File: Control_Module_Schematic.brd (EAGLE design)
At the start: 67 x 47 mm, 30 parts, among them U2 ATMEGA328P_TQFP

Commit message: Connected the FTDI232 UART chip's GND to GND
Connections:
- net GND: now also FTDI232.6
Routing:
- net GND: track 212.5 -> 237.6 mm
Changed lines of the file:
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@@
 <wire x1="54.4576" y1="27.0256" x2="54.3392" y2="27.0683" width="0.254" layer="1"/>
 <via x="35.9664" y="28.8544" extent="1-16" drill="0.3302"/>
+<contactref element="FTDI232" pad="6"/>
+<wire x1="27.8892" y1="32.9184" x2="27.8892" y2="31.7754" width="0.254" layer="1"/>
+<wire x1="21.2598" y1="39.5478" x2="27.8892" y2="32.9184" width="0.254" layer="1"/>
+<wire x1="21.2598" y1="41.8338" x2="21.2598" y2="39.5478" width="0.254" layer="1"/>
+<wire x1="20.1168" y1="42.9768" x2="21.2598" y2="41.8338" width="0.254" layer="1"/>
+<wire x1="14.6304" y1="42.9768" x2="20.1168" y2="42.9768" width="0.254" layer="1"/>
+<wire x1="11.2014" y1="39.5478" x2="14.6304" y2="42.9768" width="0.254" layer="1"/>
+<wire x1="27.8892" y1="31.7754" x2="27.94" y2="31.7246" width="0.254" layer="1"/>
+<wire x1="11.2014" y1="39.5478" x2="11.06" y2="39.37" width="0.254" layer="1"/>
 </signal>
 <signal name="N$5">

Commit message: AC solid state relay pin change
The AC SSR is now controlled by pc2 from the atmega328. The previous pin
used to control it ADC7 was not capable of producing output and it has
been rerouted to the breakout header.
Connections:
- removed net PC2: JP4.2, U2.25
- new net ADC7: JP4.2, U2.22
- net N$9: now also U2.25; no longer U2.22
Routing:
- net ADC7: track 0.00 -> 63.2 mm, vias 0 -> 3
- net N$9: track 9.58 -> 45.4 mm
- net PC2: track 28.3 -> 0.00 mm, vias 1 -> 0
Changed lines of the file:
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@@
 </class>
 </classes>
-<designrules name="oshpark-2layer">
-<description language="de">&lt;b&gt;EAGLE Design Rules&lt;/b&gt;
+<designrules name="SparkFun">
+<description language="en">&lt;b&gt;EAGLE Design Rules&lt;/b&gt;
 &lt;p&gt;
-Die Standard-Design-Rules sind so gewählt, dass sie für
-die meisten Anwendungen passen. Sollte ihre Platine
-besondere Anforderungen haben, treffen Sie die erforderlichen
-Einstellungen hier und speichern die Design Rules unter
-einem neuen Namen ab.</description>
-<description language="en">&lt;b&gt;Laen's PCB Order Design Rules&lt;/b&gt;
-&lt;p&gt;
-Please make sure your boards conform to these design rules.</description>
+The default Design Rules have been set to cover
+a wide range of applications. Your particular design
+may have different requirements, so please make the
+necessary adjustments and save your customized
+design rules under a new name.</description>
 <param name="layerSetup" value="(1*16)"/>
-<param name="mtCopper" value="0.0356mm 0.0356mm 0.0356mm 0.0356mm 0.0356mm 0.0356mm 0.0356mm 0.0356mm 0.0356mm 0.0356mm 0.0356mm 0.0356mm 0.0356mm 0.0356mm 0.0356mm 0.0356mm"/>
-<param name="mtIsolate" value="1.5011mm 0.1499mm 0.2007mm 0.1499mm 0.2007mm 0.1499mm 0.2007mm 0.1499mm 0.2007mm 0.1499mm 0.2007mm 0.1499mm 0.2007mm 0.1499mm 0.2007mm"/>
-<param name="mdWireWire" value="6mil"/>
-<param name="mdWirePad" value="6mil"/>
-<param name="mdWireVia" value="6mil"/>
-<param name="mdPadPad" value="6mil"/>
-<param name="mdPadVia" value="6mil"/>
-<param name="mdViaVia" value="6mil"/>
-<param name="mdSmdPad" value="6mil"/>
-<param name="mdSmdVia" value="6mil"/>
-<param name="mdSmdSmd" value="6mil"/>
+<param name="mtCopper" value="0.035mm 0.035mm 0.035mm 0.035mm 0.035mm 0.035mm 0.035mm 0.035mm 0.035mm 0.035mm 0.035mm 0.035mm 0.035mm 0.035mm 0.035mm 0.035mm"/>
+<param name="mtIsolate" value="1.5mm 0.15mm 0.2mm 0.15mm 0.2mm 0.15mm 0.2mm 0.15mm 0.2mm 0.15mm 0.2mm 0.15mm 0.2mm 0.15mm 0.2mm"/>
+<param name="mdWireWire" value="8mil"/>
+<param name="mdWirePad" value="8mil"/>
+<param name="mdWireVia" value="8mil"/>
+<param name="mdPadPad" value="8mil"/>
+<param name="mdPadVia" value="8mil"/>
+<param name="mdViaVia" value="8mil"/>
+<param name="mdSmdPad" value="8mil"/>
+<param name="mdSmdVia" value="8mil"/>
+<param name="mdSmdSmd" value="8mil"/>
 <param name="mdViaViaSameLayer" value="8mil"/>
 <param name="mnLayersViaInSmd" value="2"/>
-<param name="mdCopperDimension" value="15mil"/>
-<param name="mdDrill" value="6mil"/>
+<param name="mdCopperDimension" value="8mil"/>
+<param name="mdDrill" value="8mil"/>
 <param name="mdSmdStop" value="0mil"/>
-<param name="msWidth" value="6mil"/>
-<param name="msDrill" value="13mil"/>
-<param name="msMicroVia" value="13mil"/>
+<param name="msWidth" value="8mil"/>
+<param name="msDrill" value="20mil"/>
+<param name="msMicroVia" value="9.99mm"/>
 <param name="msBlindViaRatio" value="0.5"/>
 <param name="rvPadTop" value="0.25"/>
@@
 <param name="rvMicroViaOuter" value="0.25"/>
 <param name="rvMicroViaInner" value="0.25"/>
-<param name="rlMinPadTop" value="7mil"/>
+<param name="rlMinPadTop" value="12mil"/>
 <param name="rlMaxPadTop" value="20mil"/>
-<param name="rlMinPadInner" value="7mil"/>
+<param name="rlMinPadInner" value="10mil"/>
 <param name="rlMaxPadInner" value="20mil"/>
-<param name="rlMinPadBottom" value="7mil"/>
+<param name="rlMinPadBottom" value="12mil"/>
 <param name="rlMaxPadBottom" value="20mil"/>
-<param name="rlMinViaOuter" value="7mil"/>
+<param name="rlMinViaOuter" value="10mil"/>
 <param name="rlMaxViaOuter" value="20mil"/>
-<param name="rlMinViaInner" value="7mil"/>
+<param name="rlMinViaInner" value="10mil"/>
 <param name="rlMaxViaInner" value="20mil"/>
 <param name="rlMinMicroViaOuter" value="4mil"/>
@@
 <param name="mlMinCreamFrame" value="0mil"/>
 <param name="mlMaxCreamFrame" value="0mil"/>
-<param name="mlViaStopLimit" value="0mil"/>
+<param name="mlViaStopLimit" value="20mil"/>
 <param name="srRoundness" value="0"/>
 <param name="srMinRoundness" value="0mil"/>
@@
 <wire x1="54.2544" y1="29.464" x2="54.3392" y2="29.6083" width="0.254" layer="1"/>
 </signal>
-<signal name="N$9">
-<contactref element="R1" pad="1"/>
-<contactref element="U2" pad="22"/>
-<wire x1="39.624" y1="21.5392" x2="38.608" y2="21.5392" width="0.254" layer="1"/>
-<wire x1="44.704" y1="26.6192" x2="39.624" y2="21.5392" width="0.254" layer="1"/>
-<wire x1="45.9232" y1="26.6192" x2="44.704" y2="26.6192" width="0.254" layer="1"/>
-<wire x1="38.608" y1="21.5392" x2="38.5826" y2="21.52" width="0.254" layer="1"/>
-<wire x1="45.9232" y1="26.6192" x2="46.04" y2="26.67" width="0.254" layer="1"/>
-</signal>
 <signal name="N$11">
 <contactref element="SSR" pad="P$2"/>
@@
 <wire x1="54.5846" y1="42.6466" x2="54.3392" y2="42.1583" width="2.921" layer="1"/>
 <wire x1="62.1792" y1="42.8752" x2="62.23" y2="43.02" width="2.921" layer="1"/>
-</signal>
-<signal name="PC2">
-<contactref element="JP4" pad="2"/>
-<contactref element="U2" pad="25"/>
-<wire x1="37.5666" y1="25.8572" x2="37.1856" y2="24.7904" width="0.254" layer="1"/>
-<wire x1="37.3888" y1="27.3304" x2="37.5666" y2="25.8572" width="0.254" layer="1"/>
-<wire x1="37.5666" y1="25.8064" x2="37.3888" y2="27.3304" width="0.254" layer="16"/>
-<wire x1="36.9824" y1="25.6032" x2="37.5666" y2="25.8064" width="0.254" layer="16"/>
-<wire x1="36.576" y1="25.6032" x2="36.9824" y2="25.6032" width="0.254" layer="16"/>
-<wire x1="29.2608" y1="32.9184" x2="36.576" y2="25.6032" width="0.254" layer="16"/>
-<wire x1="29.2608" y1="33.1216" x2="29.2608" y2="32.9184" width="0.254" layer="16"/>
-<wire x1="23.368" y1="39.0144" x2="29.2608" y2="33.1216" width="0.254" layer="16"/>
-<wire x1="21.5392" y1="39.0144" x2="23.368" y2="39.0144" width="0.254" layer="16"/>
-<wire x1="20.1168" y1="40.4368" x2="21.5392" y2="39.0144" width="0.254" layer="16"/>
-<wire x1="37.1856" y1="24.7904" x2="37.09" y2="24.6126" width="0.254" layer="1"/>
-<wire x1="20.1168" y1="40.4368" x2="19.9517" y2="40.6146" width="0.254" layer="16"/>
-<via x="37.3888" y="27.3304" extent="1-16" drill="0.3302"/>
 </signal>
 <signal name="PC3">
@@
 <wire x1="34.925" y1="19.0754" x2="34.9504" y2="19.1008" width="0.254" layer="16"/>
 </signal>
+<signal name="N$9">
+<contactref element="U2" pad="25"/>
+<contactref element="R1" pad="1"/>
+<wire x1="37.2618" y1="25.8318" x2="37.2618" y2="24.6888" width="0.254" layer="1"/>
+<wire x1="37.4904" y1="26.0604" x2="37.2618" y2="25.8318" width="0.254" layer="1"/>
+<wire x1="37.4904" y1="35.6616" x2="37.4904" y2="26.0604" width="0.254" layer="1"/>
+<wire x1="33.8328" y1="39.3192" x2="37.4904" y2="35.6616" width="0.254" layer="1"/>
+<wire x1="33.8328" y1="41.8338" x2="33.8328" y2="39.3192" width="0.254" layer="1"/>
+<wire x1="35.8902" y1="43.8912" x2="33.8328" y2="41.8338" width="0.254" layer="1"/>
+<wire x1="39.5478" y1="43.8912" x2="35.8902" y2="43.8912" width="0.254" layer="1"/>
+<wire x1="45.9486" y1="37.4904" x2="39.5478" y2="43.8912" width="0.254" layer="1"/>
+<wire x1="45.9486" y1="26.7462" x2="45.9486" y2="37.4904" width="0.254" layer="1"/>
+<wire x1="37.2618" y1="24.6888" x2="37.09" y2="24.6126" width="0.254" layer="1"/>
+<wire x1="45.9486" y1="26.7462" x2="46.04" y2="26.67" width="0.254" layer="1"/>
+</signal>
+<signal name="ADC7">
+<contactref element="U2" pad="22"/>
+<contactref element="JP4" pad="2"/>
+<wire x1="39.3192" y1="21.4884" x2="38.6334" y2="21.4884" width="0.254" layer="1"/>
+<wire x1="44.1198" y1="26.289" x2="39.3192" y2="21.4884" width="0.254" layer="1"/>
+<wire x1="44.1198" y1="34.29" x2="44.1198" y2="26.289" width="0.254" layer="1"/>
+<wire x1="39.0906" y1="39.3192" x2="44.1198" y2="34.29" width="0.254" layer="1"/>
+<wire x1="39.0906" y1="42.9768" x2="39.0906" y2="39.3192" width="0.254" layer="1"/>
+<wire x1="38.6334" y1="42.9768" x2="39.0906" y2="42.9768" width="0.254" layer="16"/>
+<wire x1="37.9476" y1="43.6626" x2="38.6334" y2="42.9768" width="0.254" layer="16"/>
+<wire x1="16.6878" y1="43.6626" x2="37.9476" y2="43.6626" width="0.254" layer="16"/>
+<wire x1="13.2588" y1="40.2336" x2="16.6878" y2="43.6626" width="0.254" layer="16"/>
+<wire x1="15.5448" y1="40.2336" x2="13.2588" y2="40.2336" width="0.254" layer="1"/>
+<wire x1="17.8308" y1="37.9476" x2="15.5448" y2="40.2336" width="0.254" layer="1"/>
+<wire x1="18.0594" y1="37.9476" x2="17.8308" y2="37.9476" width="0.254" layer="1"/>
+<wire x1="18.0594" y1="38.4048" x2="18.0594" y2="37.9476" width="0.254" layer="16"/>
+<wire x1="20.1168" y1="40.4622" x2="18.0594" y2="38.4048" width="0.254" layer="16"/>
+<wire x1="38.6334" y1="21.4884" x2="38.5826" y2="21.52" width="0.254" layer="1"/>
+<wire x1="20.1168" y1="40.4622" x2="19.9517" y2="40.6146" width="0.254" layer="16"/>
+<via x="39.0906" y="42.9768" extent="1-16" drill="0.508"/>
+<via x="13.2588" y="40.2336" extent="1-16" drill="0.508"/>
+<via x="18.0594" y="37.9476" extent="1-16" drill="0.508"/>
+</signal>
 </signals>

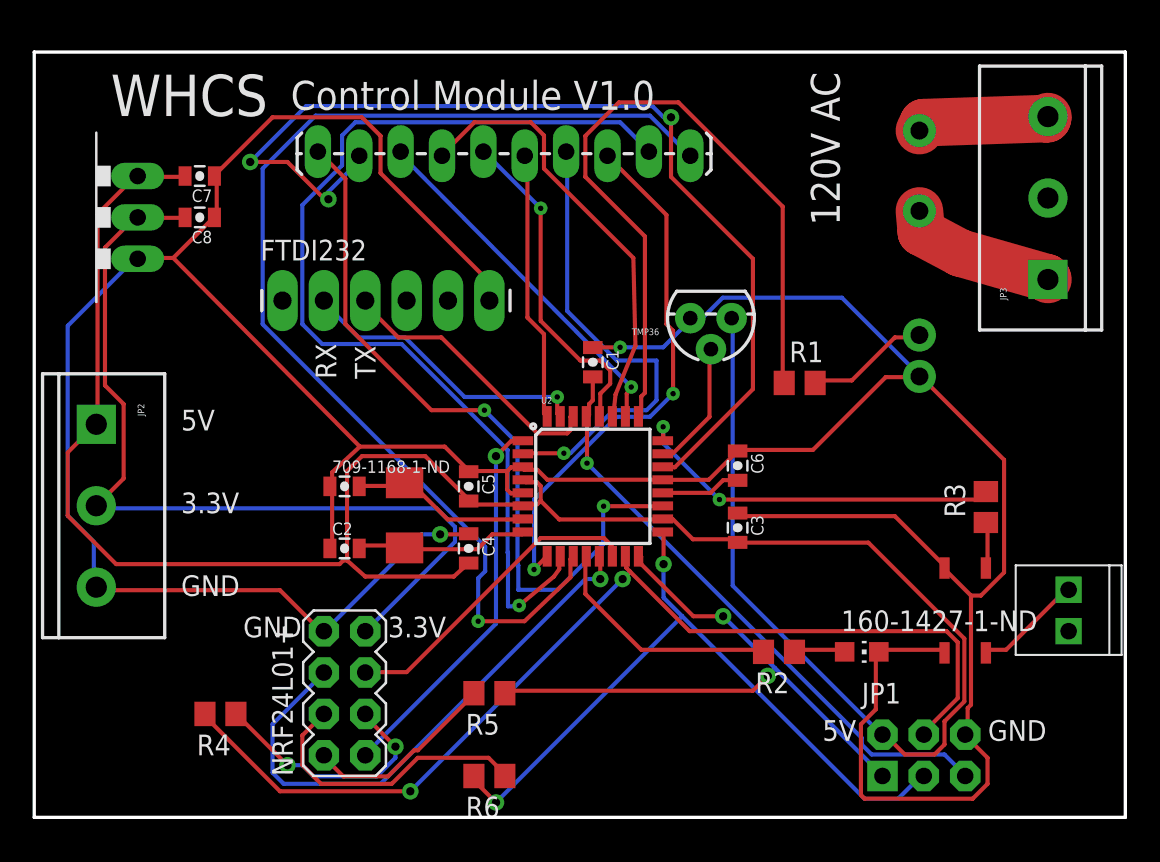
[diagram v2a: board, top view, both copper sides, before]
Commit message: Added tactile switch for reset
Also did some manual routing optimizations
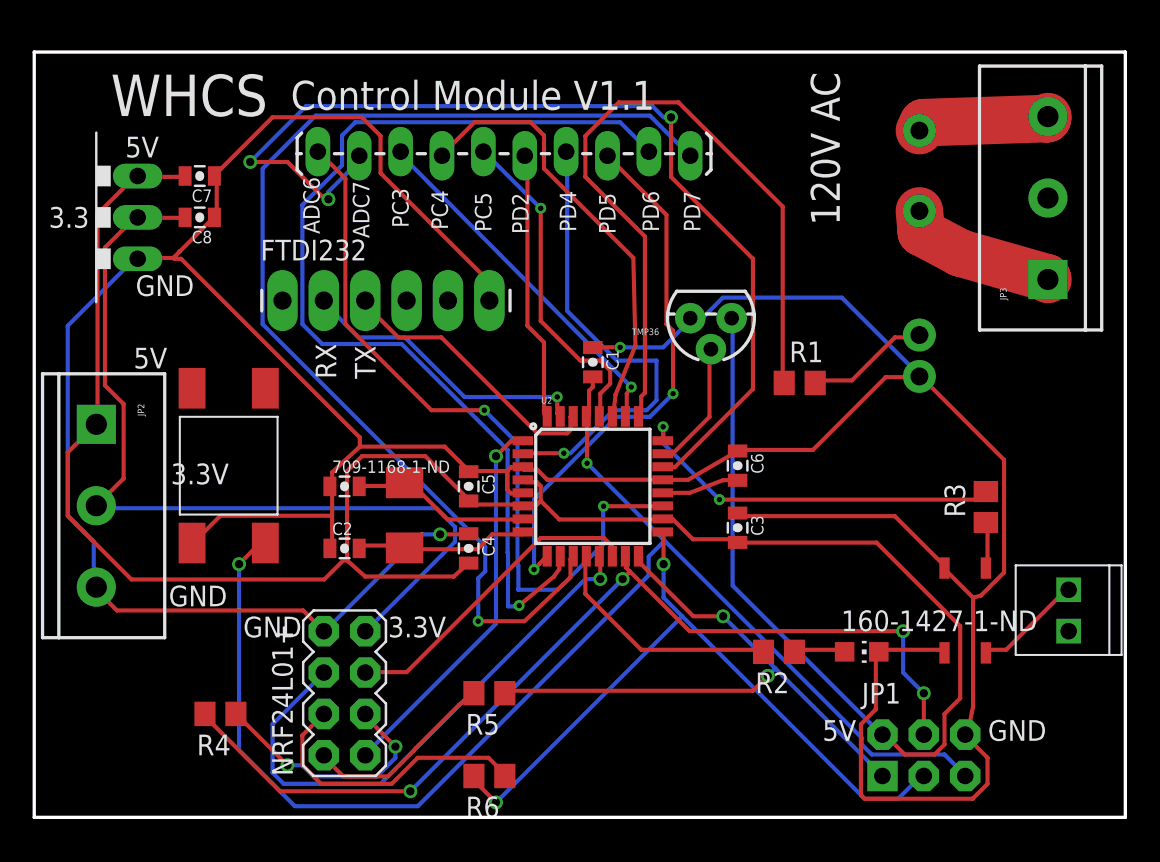
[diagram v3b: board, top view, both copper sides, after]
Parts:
- added TAC_SWITCH: TACTILE_SWITCH, WHCS:TAC_SWITCH_GULL_WING
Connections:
- net GND: now also TAC_SWITCH.P$2
- net N$24: now also TAC_SWITCH.P$4
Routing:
- net N$24: track 37.0 -> 85.6 mm, vias 1 -> 2
- net GND: track 237.6 -> 247.1 mm
- net N$3: track 63.2 -> 60.1 mm, vias 2 -> 4
- net 5V: track 144.3 -> 145.2 mm
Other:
- board text added: "3.3"
- board text added: "ADC6"
- board text added: "ADC7"
- board text added: "Control Module V1.1"
- board text added: "PC3"
- board text added: "PC4"
- board text added: "PC5"
- board text added: "PD2"
- board text added: "PD4"
- board text added: "PD5"
- board text added: "PD6"
- board text added: "PD7"
- board text removed: "Control Module V1.0"

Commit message: Final changes before placing oshpark 2nd order.
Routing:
- net ADC7: track 63.2 -> 69.5 mm
- net N$9: track 45.4 -> 47.7 mm
- net PD7: track 70.4 -> 71.4 mm
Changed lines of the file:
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@@
 <text x="6.223" y="32.004" size="1.27" layer="21">GND</text>
 <text x="0.889" y="36.195" size="1.27" layer="21">3.3</text>
+<text x="27.305" y="29.337" size="1.27" layer="21" rot="R270">GND</text>
 </plain>
 <attributes>
@@
 <contactref element="JP4" pad="5"/>
 <contactref element="U2" pad="28"/>
-<wire x1="34.7472" y1="26.0096" x2="34.7472" y2="24.7904" width="0.254" layer="1"/>
-<wire x1="35.3568" y1="26.6192" x2="34.7472" y2="26.0096" width="0.254" layer="1"/>
+<wire x1="34.7472" y1="25.8826" x2="34.7472" y2="24.7904" width="0.254" layer="1"/>
+<wire x1="35.3568" y1="26.6192" x2="34.7472" y2="25.8826" width="0.254" layer="1"/>
 <wire x1="35.3568" y1="27.432" x2="35.3568" y2="26.6192" width="0.254" layer="1"/>
 <wire x1="34.7472" y1="28.0416" x2="35.3568" y2="27.432" width="0.254" layer="1"/>
@@
 <wire x1="31.9024" y1="14.7828" x2="29.7688" y2="13.0048" width="0.254" layer="1"/>
 <wire x1="29.0576" y1="22.5552" x2="29.0576" y2="16.256" width="0.254" layer="16"/>
-<wire x1="22.5552" y1="29.0576" x2="29.0576" y2="22.5552" width="0.254" layer="16"/>
-<wire x1="17.6784" y1="29.0576" x2="22.5552" y2="29.0576" width="0.254" layer="16"/>
-<wire x1="16.4592" y1="30.2768" x2="17.6784" y2="29.0576" width="0.254" layer="16"/>
+<wire x1="22.5552" y1="28.8036" x2="29.0576" y2="22.5552" width="0.254" layer="16"/>
+<wire x1="17.8054" y1="28.8036" x2="22.5552" y2="28.8036" width="0.254" layer="16"/>
+<wire x1="16.4592" y1="30.2768" x2="17.8054" y2="28.8036" width="0.254" layer="16"/>
 <wire x1="16.4592" y1="37.592" x2="16.4592" y2="30.2768" width="0.254" layer="16"/>
 <wire x1="18.8976" y1="40.0304" x2="16.4592" y2="37.592" width="0.254" layer="16"/>
@@
 <wire x1="14.0208" y1="30.2768" x2="27.686" y2="16.6116" width="0.254" layer="16"/>
 <wire x1="14.0208" y1="39.8272" x2="14.0208" y2="30.2768" width="0.254" layer="16"/>
-<wire x1="17.272" y1="43.0784" x2="14.0208" y2="39.8272" width="0.254" layer="16"/>
-<wire x1="37.7952" y1="43.0784" x2="17.272" y2="43.0784" width="0.254" layer="16"/>
-<wire x1="40.2336" y1="40.64" x2="37.7952" y2="43.0784" width="0.254" layer="16"/>
+<wire x1="18.288" y1="44.0944" x2="14.0208" y2="39.8272" width="0.254" layer="16"/>
+<wire x1="37.2872" y1="44.0944" x2="18.288" y2="44.0944" width="0.254" layer="16"/>
+<wire x1="40.2336" y1="40.64" x2="37.2872" y2="44.0944" width="0.254" layer="16"/>
 <wire x1="32.9184" y1="15.8496" x2="33.09" y2="16.0274" width="0.254" layer="1"/>
 <wire x1="40.2336" y1="40.64" x2="40.2717" y2="40.6146" width="0.254" layer="16"/>
@@
 <wire x1="33.8328" y1="39.3192" x2="37.4904" y2="35.6616" width="0.254" layer="1"/>
 <wire x1="33.8328" y1="41.8338" x2="33.8328" y2="39.3192" width="0.254" layer="1"/>
-<wire x1="35.8902" y1="43.8912" x2="33.8328" y2="41.8338" width="0.254" layer="1"/>
-<wire x1="39.5478" y1="43.8912" x2="35.8902" y2="43.8912" width="0.254" layer="1"/>
-<wire x1="45.9486" y1="37.4904" x2="39.5478" y2="43.8912" width="0.254" layer="1"/>
+<wire x1="36.3982" y1="44.5262" x2="33.8328" y2="41.8338" width="0.254" layer="1"/>
 <wire x1="45.9486" y1="26.7462" x2="45.9486" y2="37.4904" width="0.254" layer="1"/>
 <wire x1="37.2618" y1="24.6888" x2="37.09" y2="24.6126" width="0.254" layer="1"/>
 <wire x1="45.9486" y1="26.7462" x2="46.04" y2="26.67" width="0.254" layer="1"/>
+<wire x1="36.3982" y1="44.5262" x2="41.8338" y2="44.5262" width="0.254" layer="1"/>
+<wire x1="41.8338" y1="44.5262" x2="45.72" y2="40.64" width="0.254" layer="1"/>
+<wire x1="45.72" y1="40.64" x2="45.72" y2="37.719" width="0.254" layer="1"/>
+<wire x1="45.72" y1="37.719" x2="45.9486" y2="37.4904" width="0.254" layer="1"/>
 </signal>
 <signal name="ADC7">
@@
 <wire x1="44.1198" y1="34.29" x2="44.1198" y2="26.289" width="0.254" layer="1"/>
 <wire x1="39.0906" y1="39.3192" x2="44.1198" y2="34.29" width="0.254" layer="1"/>
-<wire x1="39.0906" y1="42.9768" x2="39.0906" y2="39.3192" width="0.254" layer="1"/>
-<wire x1="38.6334" y1="42.9768" x2="39.0906" y2="42.9768" width="0.254" layer="16"/>
-<wire x1="37.9476" y1="43.6626" x2="38.6334" y2="42.9768" width="0.254" layer="16"/>
-<wire x1="16.6878" y1="43.6626" x2="37.9476" y2="43.6626" width="0.254" layer="16"/>
-<wire x1="13.2588" y1="40.2336" x2="16.6878" y2="43.6626" width="0.254" layer="16"/>
+<wire x1="39.0906" y1="43.6118" x2="39.0906" y2="39.3192" width="0.254" layer="1"/>
+<wire x1="39.0144" y1="44.8818" x2="39.0906" y2="43.6118" width="0.254" layer="16"/>
+<wire x1="17.9578" y1="44.9326" x2="37.9476" y2="44.9326" width="0.254" layer="16"/>
+<wire x1="13.2588" y1="40.2336" x2="17.9578" y2="44.9326" width="0.254" layer="16"/>
 <wire x1="15.5448" y1="40.2336" x2="13.2588" y2="40.2336" width="0.254" layer="1"/>
 <wire x1="17.8308" y1="37.9476" x2="15.5448" y2="40.2336" width="0.254" layer="1"/>
@@
 <wire x1="38.6334" y1="21.4884" x2="38.5826" y2="21.52" width="0.254" layer="1"/>
 <wire x1="20.1168" y1="40.4622" x2="19.9517" y2="40.6146" width="0.254" layer="16"/>
-<via x="39.0906" y="42.9768" extent="1-16" drill="0.508"/>
+<via x="39.0906" y="43.6118" extent="1-16" drill="0.508"/>
 <via x="13.2588" y="40.2336" extent="1-16" drill="0.508"/>
 <via x="18.0594" y="37.9476" extent="1-16" drill="0.508"/>
+<wire x1="39.0144" y1="44.8818" x2="35.8394" y2="45.0088" width="0.254" layer="16"/>
+<wire x1="35.8394" y1="45.0088" x2="37.9476" y2="44.9326" width="0.254" layer="16"/>
 </signal>
 </signals>
